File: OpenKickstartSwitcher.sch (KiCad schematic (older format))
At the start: 9 parts, among them J1 Conn_01x03, J2 Conn_01x03, U1 KS_SOCKET, U2 M27C800, U3 7400

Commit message: Fix EPROM footprint
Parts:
- U2: footprint Housings_DIP:DIP-42_W15.24mm_Socket -> OpenKickstartSwitcher:DIP-42_Socket
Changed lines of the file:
@@
 F 0 "U2" H 8125 4050 50  0000 C CNN
 F 1 "M27C800" H 8125 4250 50  0000 C CNN
-F 2 "Housings_DIP:DIP-42_W15.24mm_Socket" H 8125 4150 50  0001 C CNN
+F 2 "OpenKickstartSwitcher:DIP-42_Socket" H 8125 4150 50  0001 C CNN
 F 3 "DOCUMENTATION" H 8125 4150 50  0001 C CNN
 	1    8125 4150

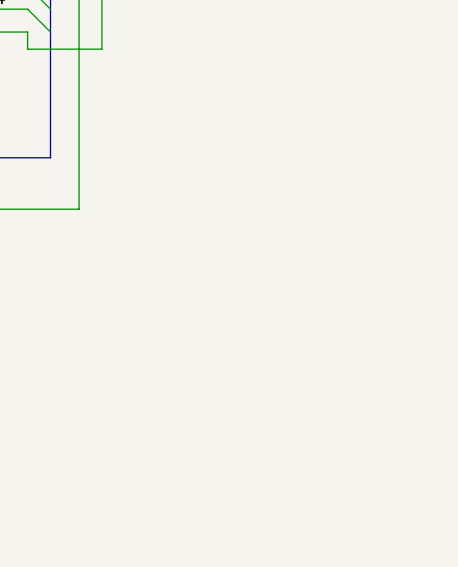
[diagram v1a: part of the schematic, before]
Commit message: Add OSHW logo and URL
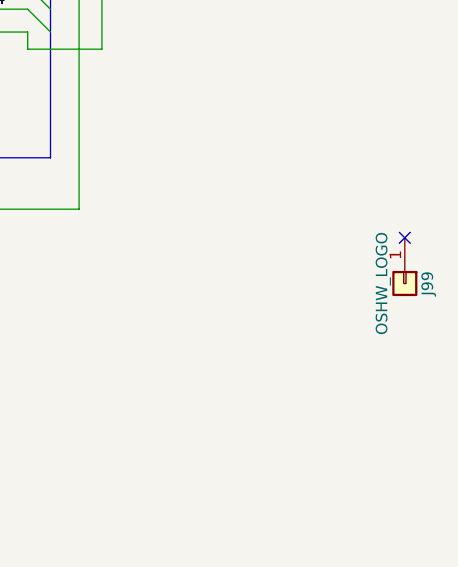
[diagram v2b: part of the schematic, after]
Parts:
- added J99: OSHW_LOGO, w_logo:Logo_copper_OSHW_6x6mm, symbol Conn_01x01
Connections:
- no-connect marks 3 -> 4
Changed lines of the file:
@@
 Wire Wire Line
 	4350 6675 4350 6750
+$Comp
+L Conn_01x01 J99
+U 1 1 5A3320D3
+P 10950 6250
+F 0 "J99" H 10950 6350 50  0000 C CNN
+F 1 "OSHW_LOGO" H 10950 6150 50  0000 C CNN
+F 2 "w_logo:Logo_copper_OSHW_6x6mm" H 10950 6250 50  0001 C CNN
+F 3 "" H 10950 6250 50  0001 C CNN
+	1    10950 6250
+	0    1    1    0
+$EndComp
+NoConn ~ 10950 6050
 $EndSCHEMATC

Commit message: Added capacitor, more space for resistors and minor adjustments
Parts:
- added C1: 100u, Capacitors_THT:C_Disc_D7.0mm_W2.5mm_P5.00mm, symbol C
- R1, R2: footprint Resistors_THT:R_Axial_DIN0204_L3.6mm_D1.6mm_P7.62mm_Horizontal -> Resistors_THT:R_Axial_DIN0207_L6.3mm_D2.5mm_P10.16mm_Horizontal
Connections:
- net GND: now also C1.2
- net VCC: now also C1.1
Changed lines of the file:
@@
 Sheet 1 1
 Title "OpenKickstartSwitcher"
-Date "2017-12-14"
+Date "2017-12-15"
 Rev "1"
 Comp "SukkoPera"
@@
 F 0 "R1" V 2430 1125 50  0000 C CNN
 F 1 "10k" V 2350 1125 50  0000 C CNN
-F 2 "Resistors_THT:R_Axial_DIN0204_L3.6mm_D1.6mm_P7.62mm_Horizontal" V 2280 1125 50  0001 C CNN
+F 2 "Resistors_THT:R_Axial_DIN0207_L6.3mm_D2.5mm_P10.16mm_Horizontal" V 2280 1125 50  0001 C CNN
 F 3 "" H 2350 1125 50  0001 C CNN
 	1    2350 1125
@@
 F 0 "R2" V 2630 1125 50  0000 C CNN
 F 1 "10k" V 2550 1125 50  0000 C CNN
-F 2 "Resistors_THT:R_Axial_DIN0204_L3.6mm_D1.6mm_P7.62mm_Horizontal" V 2480 1125 50  0001 C CNN
+F 2 "Resistors_THT:R_Axial_DIN0207_L6.3mm_D2.5mm_P10.16mm_Horizontal" V 2480 1125 50  0001 C CNN
 F 3 "" H 2550 1125 50  0001 C CNN
 	1    2550 1125
@@
 $EndComp
 NoConn ~ 10950 6050
+$Comp
+L VCC #PWR011
+U 1 1 5A343310
+P 10525 3775
+F 0 "#PWR011" H 10525 3625 50  0001 C CNN
+F 1 "VCC" H 10525 3925 50  0000 C CNN
+F 2 "" H 10525 3775 50  0001 C CNN
+F 3 "" H 10525 3775 50  0001 C CNN
+	1    10525 3775
+	1    0    0    -1
+$EndComp
+$Comp
+L C C1
+U 1 1 5A343337
+P 10525 4025
+F 0 "C1" H 10550 4125 50  0000 L CNN
+F 1 "100u" H 10550 3925 50  0000 L CNN
+F 2 "Capacitors_THT:C_Disc_D7.0mm_W2.5mm_P5.00mm" H 10563 3875 50  0001 C CNN
+F 3 "" H 10525 4025 50  0001 C CNN
+	1    10525 4025
+	1    0    0    -1
+$EndComp
+$Comp
+L GND #PWR012
+U 1 1 5A3433A6
+P 10525 4275
+F 0 "#PWR012" H 10525 4025 50  0001 C CNN
+F 1 "GND" H 10525 4125 50  0000 C CNN
+F 2 "" H 10525 4275 50  0001 C CNN
+F 3 "" H 10525 4275 50  0001 C CNN
+	1    10525 4275
+	1    0    0    -1
+$EndComp
+Wire Wire Line
+	10525 4275 10525 4175
+Wire Wire Line
+	10525 3875 10525 3775
 $EndSCHEMATC

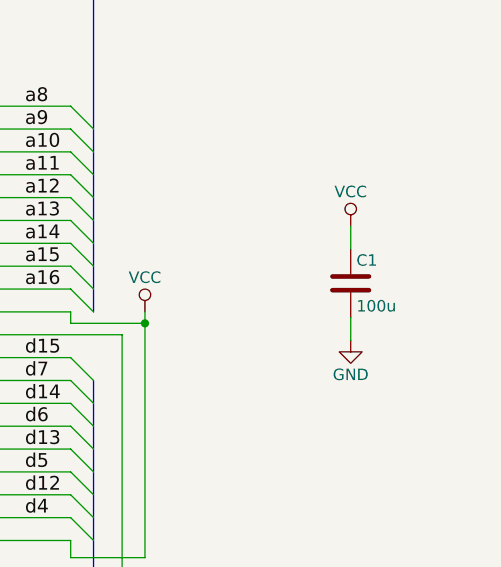
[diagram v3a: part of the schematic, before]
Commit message: Add capacitor on 7400 I don't like this too much, tracks under the 7400 are pretty messy. Let's see if we can come up with something better.
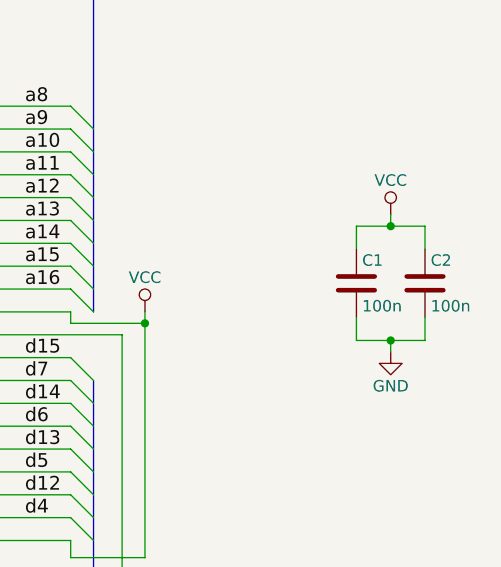
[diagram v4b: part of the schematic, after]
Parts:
- added C2: 100n, Capacitors_THT:C_Disc_D7.0mm_W2.5mm_P5.00mm, symbol C
- C1: value 100u -> 100n
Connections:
- net GND: now also C2.2
- net VCC: now also C2.1
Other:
- moved on the sheet: C1
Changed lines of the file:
@@
 Sheet 1 1
 Title "OpenKickstartSwitcher"
-Date "2017-12-15"
+Date "2017-12-17"
 Rev "1"
 Comp "SukkoPera"
@@
 	0    1    1    0
 $EndComp
+$Comp
+L Conn_01x01 J99
+U 1 1 5A3320D3
+P 10950 6250
+F 0 "J99" H 10950 6350 50  0000 C CNN
+F 1 "OSHW_LOGO" H 10950 6150 50  0000 C CNN
+F 2 "w_logo:Logo_copper_OSHW_6x6mm" H 10950 6250 50  0001 C CNN
+F 3 "" H 10950 6250 50  0001 C CNN
+	1    10950 6250
+	0    1    1    0
+$EndComp
+NoConn ~ 10950 6050
+$Comp
+L VCC #PWR011
+U 1 1 5A343310
+P 10700 3725
+F 0 "#PWR011" H 10700 3575 50  0001 C CNN
+F 1 "VCC" H 10700 3875 50  0000 C CNN
+F 2 "" H 10700 3725 50  0001 C CNN
+F 3 "" H 10700 3725 50  0001 C CNN
+	1    10700 3725
+	1    0    0    -1
+$EndComp
+$Comp
+L C C1
+U 1 1 5A343337
+P 10550 4025
+F 0 "C1" H 10575 4125 50  0000 L CNN
+F 1 "100n" H 10575 3925 50  0000 L CNN
+F 2 "Capacitors_THT:C_Disc_D7.0mm_W2.5mm_P5.00mm" H 10588 3875 50  0001 C CNN
+F 3 "" H 10550 4025 50  0001 C CNN
+	1    10550 4025
+	1    0    0    -1
+$EndComp
+$Comp
+L GND #PWR012
+U 1 1 5A3433A6
+P 10700 4325
+F 0 "#PWR012" H 10700 4075 50  0001 C CNN
+F 1 "GND" H 10700 4175 50  0000 C CNN
+F 2 "" H 10700 4325 50  0001 C CNN
+F 3 "" H 10700 4325 50  0001 C CNN
+	1    10700 4325
+	1    0    0    -1
+$EndComp
+$Comp
+L C C2
+U 1 1 5A36EFAF
+P 10850 4025
+F 0 "C2" H 10875 4125 50  0000 L CNN
+F 1 "100n" H 10875 3925 50  0000 L CNN
+F 2 "Capacitors_THT:C_Disc_D7.0mm_W2.5mm_P5.00mm" H 10888 3875 50  0001 C CNN
+F 3 "" H 10850 4025 50  0001 C CNN
+	1    10850 4025
+	1    0    0    -1
+$EndComp
 Wire Wire Line
 	6750 4250 7375 4250
@@
 Wire Wire Line
 	4350 6675 4350 6750
-$Comp
-L Conn_01x01 J99
-U 1 1 5A3320D3
-P 10950 6250
-F 0 "J99" H 10950 6350 50  0000 C CNN
-F 1 "OSHW_LOGO" H 10950 6150 50  0000 C CNN
-F 2 "w_logo:Logo_copper_OSHW_6x6mm" H 10950 6250 50  0001 C CNN
-F 3 "" H 10950 6250 50  0001 C CNN
-	1    10950 6250
-	0    1    1    0
-$EndComp
-NoConn ~ 10950 6050
-$Comp
-L VCC #PWR011
-U 1 1 5A343310
-P 10525 3775
-F 0 "#PWR011" H 10525 3625 50  0001 C CNN
-F 1 "VCC" H 10525 3925 50  0000 C CNN
-F 2 "" H 10525 3775 50  0001 C CNN
-F 3 "" H 10525 3775 50  0001 C CNN
-	1    10525 3775
-	1    0    0    -1
-$EndComp
-$Comp
-L C C1
-U 1 1 5A343337
-P 10525 4025
-F 0 "C1" H 10550 4125 50  0000 L CNN
-F 1 "100u" H 10550 3925 50  0000 L CNN
-F 2 "Capacitors_THT:C_Disc_D7.0mm_W2.5mm_P5.00mm" H 10563 3875 50  0001 C CNN
-F 3 "" H 10525 4025 50  0001 C CNN
-	1    10525 4025
-	1    0    0    -1
-$EndComp
-$Comp
-L GND #PWR012
-U 1 1 5A3433A6
-P 10525 4275
-F 0 "#PWR012" H 10525 4025 50  0001 C CNN
-F 1 "GND" H 10525 4125 50  0000 C CNN
-F 2 "" H 10525 4275 50  0001 C CNN
-F 3 "" H 10525 4275 50  0001 C CNN
-	1    10525 4275
-	1    0    0    -1
-$EndComp
-Wire Wire Line
-	10525 4275 10525 4175
-Wire Wire Line
-	10525 3875 10525 3775
+Wire Wire Line
+	10550 4275 10550 4175
+Wire Wire Line
+	10550 3875 10550 3775
+Wire Wire Line
+	10550 3775 10850 3775
+Wire Wire Line
+	10850 3775 10850 3875
+Wire Wire Line
+	10700 3725 10700 3775
+Connection ~ 10700 3775
+Wire Wire Line
+	10550 4275 10850 4275
+Wire Wire Line
+	10850 4275 10850 4175
+Wire Wire Line
+	10700 4275 10700 4325
+Connection ~ 10700 4275
 $EndSCHEMATC

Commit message: Much better now :)
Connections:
- net VCC: now also U3.10; no longer U3.5
- net sw17: now also U3.13; no longer U3.10
- net sw18: now also U3.5, U3.9; no longer U3.1, U3.4
- net at U2.2 (A17): now also U3.3; no longer U3.11
- net at U3.2: now also U3.11; no longer J1.2 (Pin_2)
- net at U3.12: now also U3.8; no longer U3.3
- net at U3.6: now also U3.1; no longer U3.9
- new net a17: J1.2 (Pin_2), U3.4
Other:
- moved on the sheet: C1, C2, U3A, U3B, U3C, U3D
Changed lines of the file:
@@
 L 7400 U3
 U 1 1 5A2F1A87
+P 6625 1500
+F 0 "U3" H 6625 1550 50  0000 C CNN
+F 1 "7400" H 6625 1400 50  0000 C CNN
+F 2 "Housings_DIP:DIP-14_W7.62mm" H 6625 1500 50  0001 C CNN
+F 3 "" H 6625 1500 50  0001 C CNN
+	1    6625 1500
+	1    0    0    -1
+$EndComp
+$Comp
+L 7400 U3
+U 2 1 5A2F1BDC
 P 3925 1175
 F 0 "U3" H 3925 1225 50  0000 C CNN
@@
 F 2 "Housings_DIP:DIP-14_W7.62mm" H 3925 1175 50  0001 C CNN
 F 3 "" H 3925 1175 50  0001 C CNN
-	1    3925 1175
+	2    3925 1175
 	1    0    0    -1
 $EndComp
 $Comp
 L 7400 U3
-U 2 1 5A2F1BDC
+U 3 1 5A2F1C7F
 P 3925 1825
 F 0 "U3" H 3925 1875 50  0000 C CNN
@@
 F 2 "Housings_DIP:DIP-14_W7.62mm" H 3925 1825 50  0001 C CNN
 F 3 "" H 3925 1825 50  0001 C CNN
-	2    3925 1825
+	3    3925 1825
 	1    0    0    -1
 $EndComp
 $Comp
 L 7400 U3
-U 3 1 5A2F1C7F
+U 4 1 5A2F1D22
 P 5225 1925
 F 0 "U3" H 5225 1975 50  0000 C CNN
@@
 F 2 "Housings_DIP:DIP-14_W7.62mm" H 5225 1925 50  0001 C CNN
 F 3 "" H 5225 1925 50  0001 C CNN
-	3    5225 1925
-	1    0    0    -1
-$EndComp
-$Comp
-L 7400 U3
-U 4 1 5A2F1D22
-P 6625 1500
-F 0 "U3" H 6625 1550 50  0000 C CNN
-F 1 "7400" H 6625 1400 50  0000 C CNN
-F 2 "Housings_DIP:DIP-14_W7.62mm" H 6625 1500 50  0001 C CNN
-F 3 "" H 6625 1500 50  0001 C CNN
-	4    6625 1500
+	4    5225 1925
 	1    0    0    -1
 $EndComp
@@
 Text Label 2975 2150 0    60   ~ 0
 sw17
-Text Label 2775 1075 0    60   ~ 0
-sw18
 Text Notes 7425 1450 0    60   ~ 0
 sw18 H -> a17 -> 512 KB image (2.x/3.x)\nsw18 L -> sw17 -> 2 * 256 KB images (1.x)
@@
 L VCC #PWR011
 U 1 1 5A343310
-P 10700 3725
-F 0 "#PWR011" H 10700 3575 50  0001 C CNN
-F 1 "VCC" H 10700 3875 50  0000 C CNN
-F 2 "" H 10700 3725 50  0001 C CNN
-F 3 "" H 10700 3725 50  0001 C CNN
-	1    10700 3725
+P 6175 6750
+F 0 "#PWR011" H 6175 6600 50  0001 C CNN
+F 1 "VCC" H 6175 6900 50  0000 C CNN
+F 2 "" H 6175 6750 50  0001 C CNN
+F 3 "" H 6175 6750 50  0001 C CNN
+	1    6175 6750
 	1    0    0    -1
 $EndComp
@@
 L C C1
 U 1 1 5A343337
-P 10550 4025
-F 0 "C1" H 10575 4125 50  0000 L CNN
-F 1 "100n" H 10575 3925 50  0000 L CNN
-F 2 "Capacitors_THT:C_Disc_D7.0mm_W2.5mm_P5.00mm" H 10588 3875 50  0001 C CNN
-F 3 "" H 10550 4025 50  0001 C CNN
-	1    10550 4025
+P 6025 7050
+F 0 "C1" H 6050 7150 50  0000 L CNN
+F 1 "100n" H 6050 6950 50  0000 L CNN
+F 2 "Capacitors_THT:C_Disc_D7.0mm_W2.5mm_P5.00mm" H 6063 6900 50  0001 C CNN
+F 3 "" H 6025 7050 50  0001 C CNN
+	1    6025 7050
 	1    0    0    -1
 $EndComp
@@
 L GND #PWR012
 U 1 1 5A3433A6
-P 10700 4325
-F 0 "#PWR012" H 10700 4075 50  0001 C CNN
-F 1 "GND" H 10700 4175 50  0000 C CNN
-F 2 "" H 10700 4325 50  0001 C CNN
-F 3 "" H 10700 4325 50  0001 C CNN
-	1    10700 4325
+P 6175 7350
+F 0 "#PWR012" H 6175 7100 50  0001 C CNN
+F 1 "GND" H 6175 7200 50  0000 C CNN
+F 2 "" H 6175 7350 50  0001 C CNN
+F 3 "" H 6175 7350 50  0001 C CNN
+	1    6175 7350
 	1    0    0    -1
 $EndComp
@@
 L C C2
 U 1 1 5A36EFAF
-P 10850 4025
-F 0 "C2" H 10875 4125 50  0000 L CNN
-F 1 "100n" H 10875 3925 50  0000 L CNN
-F 2 "Capacitors_THT:C_Disc_D7.0mm_W2.5mm_P5.00mm" H 10888 3875 50  0001 C CNN
-F 3 "" H 10850 4025 50  0001 C CNN
-	1    10850 4025
+P 6325 7050
+F 0 "C2" H 6350 7150 50  0000 L CNN
+F 1 "100n" H 6350 6950 50  0000 L CNN
+F 2 "Capacitors_THT:C_Disc_D7.0mm_W2.5mm_P5.00mm" H 6363 6900 50  0001 C CNN
+F 3 "" H 6325 7050 50  0001 C CNN
+	1    6325 7050
 	1    0    0    -1
 $EndComp
@@
 	2275 1400 2775 1400
 Wire Wire Line
-	2775 1075 2775 2825
-Wire Wire Line
-	2775 1075 3325 1075
-Wire Wire Line
-	3325 1275 2875 1275
-Wire Wire Line
-	3075 1075 3075 1725
+	2775 1275 2775 2825
+Wire Wire Line
+	2875 1075 3325 1075
+Wire Wire Line
+	3075 1275 3075 1725
 Wire Wire Line
 	3075 1725 3325 1725
-Connection ~ 3075 1075
 Wire Wire Line
 	4525 1825 4625 1825
@@
 	1925 2925 2875 2925
 Wire Wire Line
-	2875 2925 2875 1275
+	2875 2925 2875 1075
 Wire Wire Line
 	2025 3000 2025 3150
@@
 	4350 6675 4350 6750
 Wire Wire Line
-	10550 4275 10550 4175
-Wire Wire Line
-	10550 3875 10550 3775
-Wire Wire Line
-	10550 3775 10850 3775
-Wire Wire Line
-	10850 3775 10850 3875
-Wire Wire Line
-	10700 3725 10700 3775
-Connection ~ 10700 3775
-Wire Wire Line
-	10550 4275 10850 4275
-Wire Wire Line
-	10850 4275 10850 4175
-Wire Wire Line
-	10700 4275 10700 4325
-Connection ~ 10700 4275
+	6025 7300 6025 7200
+Wire Wire Line
+	6025 6900 6025 6800
+Wire Wire Line
+	6025 6800 6325 6800
+Wire Wire Line
+	6325 6800 6325 6900
+Wire Wire Line
+	6175 6750 6175 6800
+Connection ~ 6175 6800
+Wire Wire Line
+	6025 7300 6325 7300
+Wire Wire Line
+	6325 7300 6325 7200
+Wire Wire Line
+	6175 7300 6175 7350
+Connection ~ 6175 7300
+Wire Wire Line
+	2775 1275 3325 1275
+Text Label 2775 1750 1    60   ~ 0
+sw18
+Connection ~ 3075 1275
+Text Label 2875 1075 0    60   ~ 0
+a17
 $EndSCHEMATC
